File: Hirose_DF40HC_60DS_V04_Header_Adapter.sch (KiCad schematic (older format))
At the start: 4 parts, among them J1 DF40HC_4.0_-60DS-0.4V_51_, J2 Conn_02x30_Odd_Even

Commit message: Update degsign after gerbers generation
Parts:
- H1, H2: footprint (none) -> MountingHole:MountingHole_3.2mm_M3
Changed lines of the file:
@@
 F 0 "H1" H 3150 6296 50  0000 L CNN
 F 1 "MountingHole" H 3150 6205 50  0000 L CNN
-F 2 "" H 3050 6250 50  0001 C CNN
+F 2 "MountingHole:MountingHole_3.2mm_M3" H 3050 6250 50  0001 C CNN
 F 3 "~" H 3050 6250 50  0001 C CNN
 	1    3050 6250
@@
 F 0 "H2" H 5150 6346 50  0000 L CNN
 F 1 "MountingHole" H 5150 6255 50  0000 L CNN
-F 2 "" H 5050 6300 50  0001 C CNN
+F 2 "MountingHole:MountingHole_3.2mm_M3" H 5050 6300 50  0001 C CNN
 F 3 "~" H 5050 6300 50  0001 C CNN
 	1    5050 6300

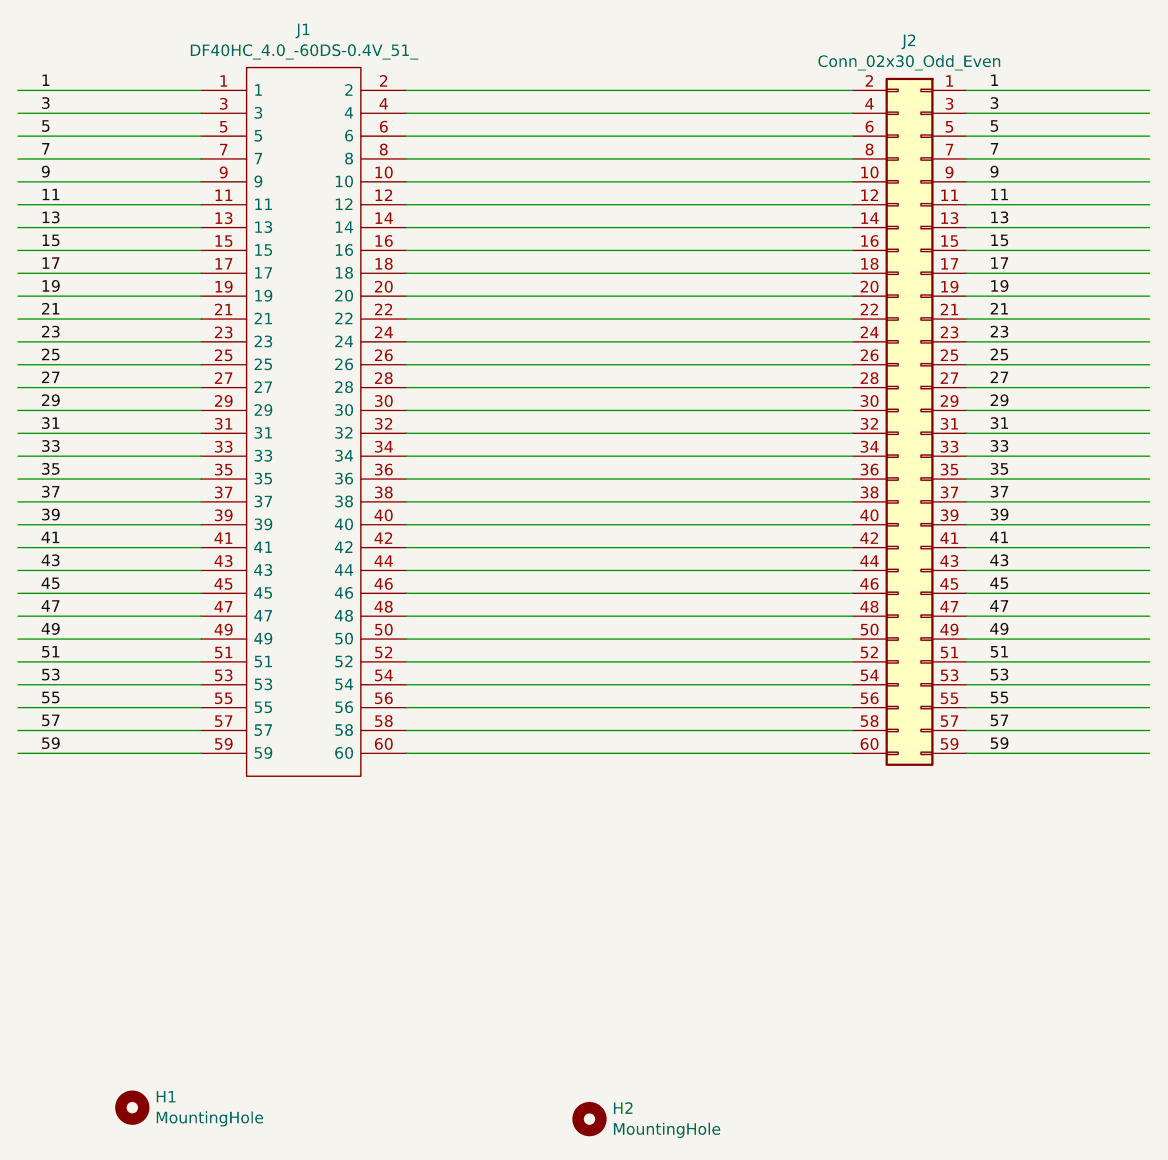
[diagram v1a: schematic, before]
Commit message: Update footprints
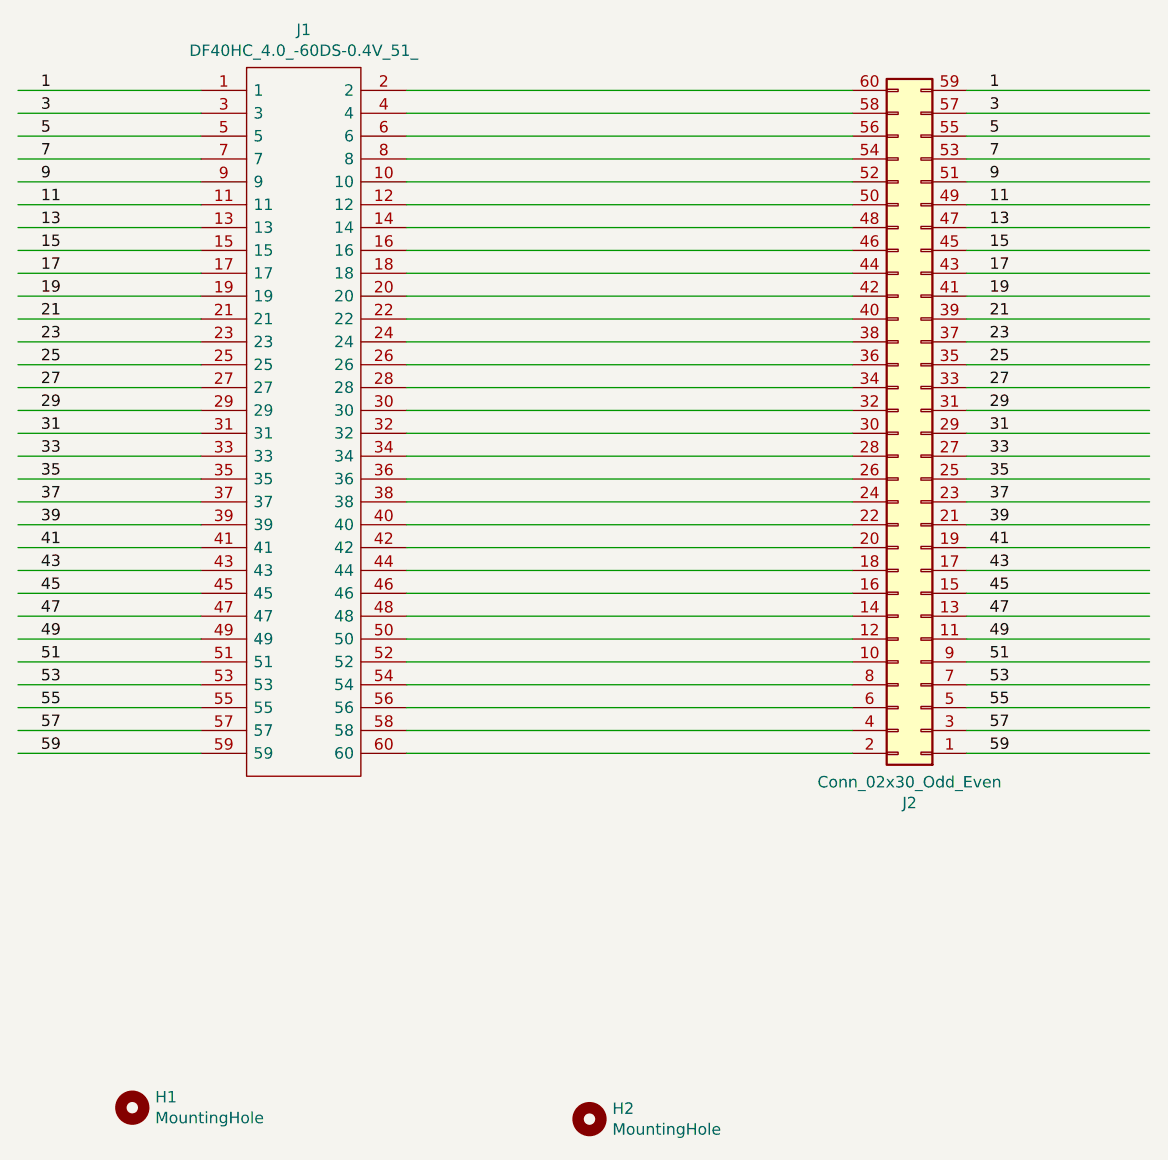
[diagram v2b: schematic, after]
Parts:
- J1: footprint footprints:DF40HC4060DS04V51 -> footprints:DF40C-60DP-0.4V_51_
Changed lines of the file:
@@
 Wire Wire Line
 	6200 4700 4250 4700
-$Comp
-L Connector_Generic:Conn_02x30_Odd_Even J2
-U 1 1 60D02385
-P 6500 3200
-F 0 "J2" H 6550 4817 50  0000 C CNN
-F 1 "Conn_02x30_Odd_Even" H 6550 4726 50  0000 C CNN
-F 2 "Connector_PinHeader_2.54mm:PinHeader_2x30_P2.54mm_Vertical" H 6500 3200 50  0001 C CNN
-F 3 "~" H 6500 3200 50  0001 C CNN
-	1    6500 3200
-	-1   0    0    -1
-$EndComp
-$Comp
-L DF40HC_4.0_-60DS-0.4V_51_:DF40HC_4.0_-60DS-0.4V_51_ J1
-U 1 1 60CFEF23
-P 3350 1800
-F 0 "J1" H 3800 2065 50  0000 C CNN
-F 1 "DF40HC_4.0_-60DS-0.4V_51_" H 3800 1974 50  0000 C CNN
-F 2 "footprints:DF40HC4060DS04V51" H 4100 1900 50  0001 L CNN
-F 3 "https://www.hirose.com/product/en/products/DF40/DF40HC%284.0%29-60DS-0.4V%2851%29/" H 4100 1800 50  0001 L CNN
-F 4 "HIROSE(HRS) - DF40HC(4.0)-60DS-0.4V(51) - CONNECTOR, STACKING, RCPT, 60POS, 2ROW" H 4100 1700 50  0001 L CNN "Description"
-F 5 "4.05" H 4100 1600 50  0001 L CNN "Height"
-F 6 "Hirose" H 4100 1500 50  0001 L CNN "Manufacturer_Name"
-F 7 "DF40HC(4.0)-60DS-0.4V(51)" H 4100 1400 50  0001 L CNN "Manufacturer_Part_Number"
-F 8 "DF40HC(4.0)-60DS-0.4V(51)" H 4100 1300 50  0001 L CNN "Arrow Part Number"
-F 9 "" H 4100 1200 50  0001 L CNN "Arrow Price/Stock"
-F 10 "798-DF4HC4060DS04V51" H 4100 1100 50  0001 L CNN "Mouser Part Number"
-F 11 "https://www.mouser.co.uk/ProductDetail/Hirose-Connector/DF40HC40-60DS-04V51?qs=tTj%252BmQ3KZwaX4XEhNHDCqg%3D%3D" H 4100 1000 50  0001 L CNN "Mouser Price/Stock"
-	1    3350 1800
-	1    0    0    -1
-$EndComp
 Text Label 2650 4700 0    50   ~ 0
 59
@@
 Text Label 6800 1800 0    50   ~ 0
 1
-Wire Wire Line
-	7500 4700 6700 4700
-Wire Wire Line
-	7500 4600 6700 4600
-Wire Wire Line
-	7500 4500 6700 4500
-Wire Wire Line
-	7500 4400 6700 4400
-Wire Wire Line
-	7500 4300 6700 4300
-Wire Wire Line
-	7500 4200 6700 4200
-Wire Wire Line
-	7500 4100 6700 4100
-Wire Wire Line
-	7500 4000 6700 4000
-Wire Wire Line
-	7500 3900 6700 3900
-Wire Wire Line
-	7500 3800 6700 3800
-Wire Wire Line
-	7500 3700 6700 3700
-Wire Wire Line
-	7500 3600 6700 3600
-Wire Wire Line
-	7500 3500 6700 3500
-Wire Wire Line
-	7500 3400 6700 3400
-Wire Wire Line
-	7500 3300 6700 3300
-Wire Wire Line
-	7500 3200 6700 3200
-Wire Wire Line
-	7500 3100 6700 3100
-Wire Wire Line
-	7500 3000 6700 3000
-Wire Wire Line
-	7500 2900 6700 2900
-Wire Wire Line
-	7500 2800 6700 2800
-Wire Wire Line
-	7500 2700 6700 2700
-Wire Wire Line
-	7500 2600 6700 2600
-Wire Wire Line
-	7500 2500 6700 2500
-Wire Wire Line
-	7500 2400 6700 2400
-Wire Wire Line
-	7500 2300 6700 2300
-Wire Wire Line
-	7500 2200 6700 2200
-Wire Wire Line
-	7500 2100 6700 2100
-Wire Wire Line
-	7500 2000 6700 2000
-Wire Wire Line
-	7500 1900 6700 1900
-Wire Wire Line
-	7500 1800 6700 1800
 $Comp
 L Mechanical:MountingHole H1
@@
 	1    0    0    -1
 $EndComp
+Wire Wire Line
+	7500 1800 6700 1800
+Wire Wire Line
+	7500 1900 6700 1900
+Wire Wire Line
+	7500 2000 6700 2000
+Wire Wire Line
+	7500 2100 6700 2100
+Wire Wire Line
+	7500 2200 6700 2200
+Wire Wire Line
+	7500 2300 6700 2300
+Wire Wire Line
+	7500 2400 6700 2400
+Wire Wire Line
+	7500 2500 6700 2500
+Wire Wire Line
+	7500 2600 6700 2600
+Wire Wire Line
+	7500 2700 6700 2700
+Wire Wire Line
+	7500 2800 6700 2800
+Wire Wire Line
+	7500 2900 6700 2900
+Wire Wire Line
+	7500 3000 6700 3000
+Wire Wire Line
+	7500 3100 6700 3100
+Wire Wire Line
+	7500 3200 6700 3200
+Wire Wire Line
+	7500 3300 6700 3300
+Wire Wire Line
+	7500 3400 6700 3400
+Wire Wire Line
+	7500 3500 6700 3500
+Wire Wire Line
+	7500 3600 6700 3600
+Wire Wire Line
+	7500 3700 6700 3700
+Wire Wire Line
+	7500 3800 6700 3800
+Wire Wire Line
+	7500 3900 6700 3900
+Wire Wire Line
+	7500 4000 6700 4000
+Wire Wire Line
+	7500 4100 6700 4100
+Wire Wire Line
+	7500 4200 6700 4200
+Wire Wire Line
+	7500 4300 6700 4300
+Wire Wire Line
+	7500 4400 6700 4400
+Wire Wire Line
+	7500 4500 6700 4500
+Wire Wire Line
+	7500 4600 6700 4600
+Wire Wire Line
+	7500 4700 6700 4700
+$Comp
+L Connector_Generic:Conn_02x30_Odd_Even J2
+U 1 1 60D02385
+P 6500 3300
+F 0 "J2" H 6550 4917 50  0000 C CNN
+F 1 "Conn_02x30_Odd_Even" H 6550 4826 50  0000 C CNN
+F 2 "Connector_PinHeader_2.54mm:PinHeader_2x30_P2.54mm_Vertical" H 6500 3300 50  0001 C CNN
+F 3 "~" H 6500 3300 50  0001 C CNN
+	1    6500 3300
+	-1   0    0    1
+$EndComp
+$Comp
+L DF40HC_4.0_-60DS-0.4V_51_:DF40HC_4.0_-60DS-0.4V_51_ J1
+U 1 1 61A23D14
+P 3350 1800
+F 0 "J1" H 3800 2065 50  0000 C CNN
+F 1 "DF40HC_4.0_-60DS-0.4V_51_" H 3800 1974 50  0000 C CNN
+F 2 "footprints:DF40C-60DP-0.4V_51_" H 4100 1900 50  0001 L CNN
+F 3 "https://www.hirose.com/product/en/products/DF40/DF40HC%284.0%29-60DS-0.4V%2851%29/" H 4100 1800 50  0001 L CNN
+F 4 "HIROSE(HRS) - DF40HC(4.0)-60DS-0.4V(51) - CONNECTOR, STACKING, RCPT, 60POS, 2ROW" H 4100 1700 50  0001 L CNN "Description"
+F 5 "4.05" H 4100 1600 50  0001 L CNN "Height"
+F 6 "Hirose" H 4100 1500 50  0001 L CNN "Manufacturer_Name"
+F 7 "DF40HC(4.0)-60DS-0.4V(51)" H 4100 1400 50  0001 L CNN "Manufacturer_Part_Number"
+F 8 "DF40HC(4.0)-60DS-0.4V(51)" H 4100 1300 50  0001 L CNN "Arrow Part Number"
+F 9 "" H 4100 1200 50  0001 L CNN "Arrow Price/Stock"
+F 10 "798-DF4HC4060DS04V51" H 4100 1100 50  0001 L CNN "Mouser Part Number"
+F 11 "https://www.mouser.co.uk/ProductDetail/Hirose-Connector/DF40HC40-60DS-04V51?qs=tTj%252BmQ3KZwaX4XEhNHDCqg%3D%3D" H 4100 1000 50  0001 L CNN "Mouser Price/Stock"
+	1    3350 1800
+	1    0    0    -1
+$EndComp
